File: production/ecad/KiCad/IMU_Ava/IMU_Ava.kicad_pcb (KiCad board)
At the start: 2 copper layers, 8 parts, among them J1 Conn_01x04_Socket, U1 BMI088

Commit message: PCB IMU
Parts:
- moved TP2 10.3 mm to (139.5, 88.5)
- moved C1 9.67 mm to (133.0, 90.0), turned to 180 degrees
- moved R1 9.65 mm to (143.0, 90.0)
- moved C2 9.58 mm to (133.0, 93.5), turned to 180 degrees
- moved R2 9.26 mm to (143.0, 93.5)
- moved J1 8.09 mm to (141.8, 85.0), turned to 180 degrees
- moved TP1 5.69 mm to (136.5, 88.5)
- moved U1 1.04 mm to (138.0, 92.9), turned to 90 degrees
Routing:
- net +3.3V: track 0.00 -> 11.5 mm
- net GND: track 0.00 -> 10.5 mm, vias 0 -> 4
- net /SDA: track 0.00 -> 7.36 mm
- net /SCL: track 0.00 -> 6.72 mm
- net Net-(U1-SDO2): track 0.00 -> 3.63 mm
- net Net-(U1-SDO1): track 0.00 -> 3.21 mm
- added copper zone on F.Cu, net +3.3V
- added copper zone on B.Cu, net GND

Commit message: silkscreen IMU PCB
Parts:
- added G***: LOGO, LOGO, B.Cu at (142.9, 93.4)
- added G***: LOGO, LOGO, B.Cu at (136.9, 89.4)

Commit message: add schematic, pullup resistors
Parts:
- added R3: 10k, Resistor_SMD:R_0805_2012Metric_Pad1.20x1.40mm_HandSolder, B.Cu at (136.0, 88.8)
- added R4: 10k, Resistor_SMD:R_0805_2012Metric_Pad1.20x1.40mm_HandSolder, B.Cu at (140.0, 88.8)
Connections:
- U1 pad 14: +3.3V -> Net-(U1-CSB1)
- U1 pad 7: +3.3V -> Net-(U1-PS)
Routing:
- net Net-(U1-CSB1): track 0.00 -> 5.11 mm, vias 0 -> 1
- net Net-(U1-PS): track 0.00 -> 2.61 mm, vias 0 -> 1
- net +3.3V: track 11.5 -> 9.08 mm, vias 0 -> 2
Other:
- board outline added: 15 x 13.5 mm

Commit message: small fixes IMU board
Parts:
- removed the G*** at (142.9, 93.4)

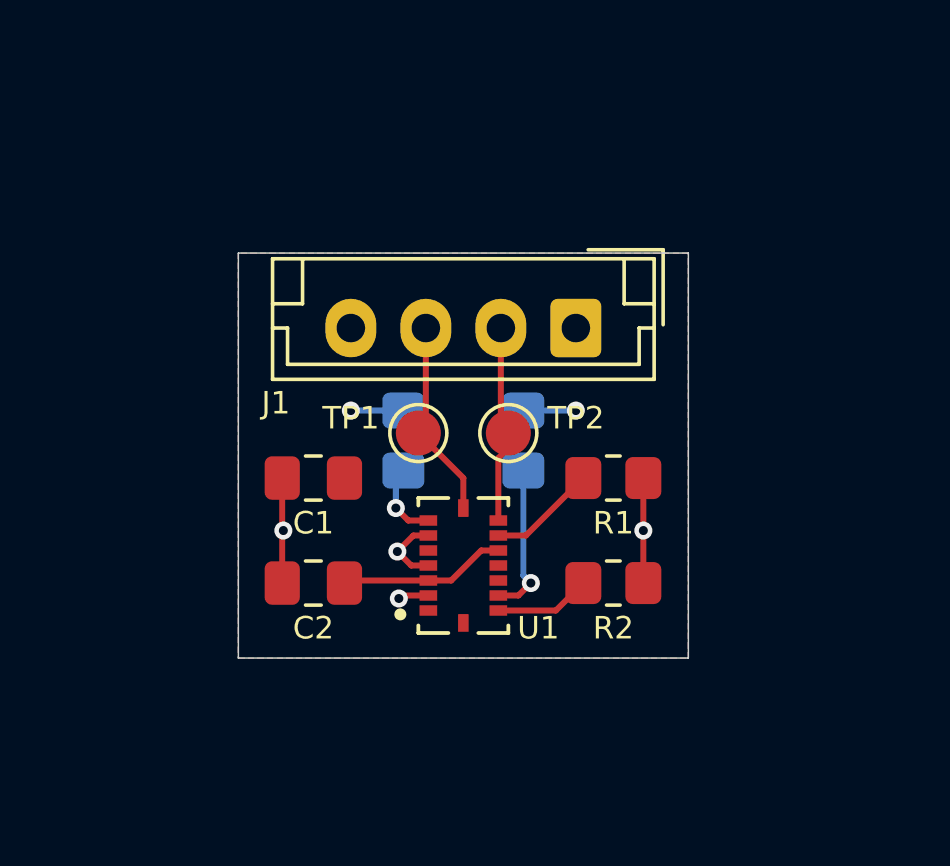
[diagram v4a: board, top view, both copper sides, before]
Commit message: IMU 90 deg conn, fixes
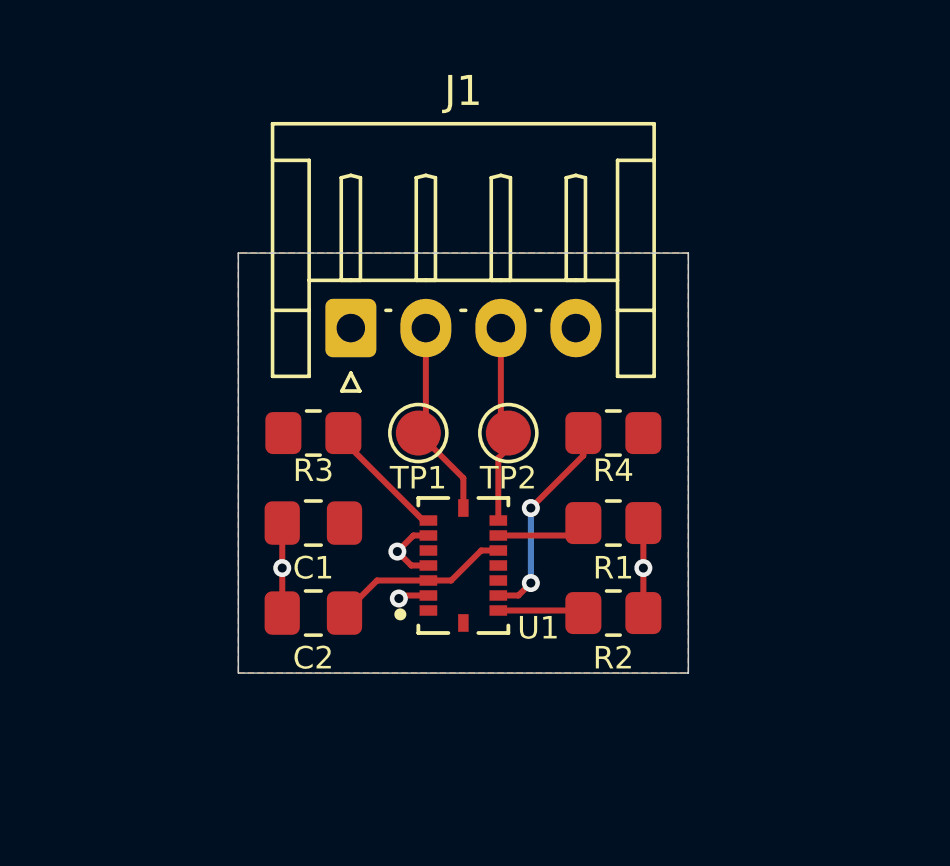
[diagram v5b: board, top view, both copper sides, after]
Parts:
- J1: footprint Connector_JST:JST_EH_B4B-EH-A_1x04_P2.50mm_Vertical -> Connector_JST:JST_EH_S4B-EH_1x04_P2.50mm_Horizontal
- R3, R4: moved to F.Cu
- moved J1 7.50 mm to (134.2, 85.0), turned to 0 degrees
- moved R3 3.01 mm to (133.0, 88.5), turned to 0 degrees
- moved R4 3.01 mm to (143.0, 88.5), turned to 180 degrees
- moved C1 1.50 mm to (133.0, 91.5)
- moved R1 1.50 mm to (143.0, 91.5)
- moved G*** 1.10 mm to (137.0, 90.5)
- moved C2 1.00 mm to (133.0, 94.5)
- moved R2 1.00 mm to (143.0, 94.5)
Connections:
- J1 pad 2: /SDA -> /SCL
- J1 pad 3: /SCL -> /SDA
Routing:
- net +3.3V: track 9.08 -> 5.89 mm, vias 2 -> 0
- net Net-(U1-CSB1): track 5.11 -> 6.98 mm, vias 1 -> 2
- net Net-(U1-PS): track 2.61 -> 3.94 mm, vias 1 -> 0
- net GND: track 10.5 -> 9.51 mm
- net Net-(U1-SDO2): track 3.63 -> 3.01 mm
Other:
- board size 15 x 13.5 mm -> 15 x 14 mm

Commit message: added mounting holes and fixed warnings
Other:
- board size 15 x 14 mm -> 27.1 x 23.9 mm
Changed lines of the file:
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@@
 			(effects
 				(font
-					(size 0.75 0.75)
+					(size 0.8 0.8)
 					(thickness 0.1)
 				)
@@
 			(effects
 				(font
-					(size 0.75 0.75)
+					(size 0.8 0.8)
 					(thickness 0.1)
 				)
@@
 		(tags "connector JST EH horizontal")
 		(property "Reference" "J1"
-			(at 3.75 -7.9 0)
+			(at 3.68 -4.91 0)
 			(layer "F.SilkS")
 			(effects
@@
 		(tags "resistor handsolder")
 		(property "Reference" "R4"
-			(at 0 -1.25 180)
+			(at 0 -1.49 180)
 			(layer "F.SilkS")
 			(effects
 				(font
-					(size 0.75 0.75)
+					(size 0.8 0.8)
 					(thickness 0.1)
 				)
@@
 		(at 138 92.915 90)
 		(property "Reference" "U1"
-			(at -2.085 2.5 180)
+			(at -3.045 0.06 180)
 			(layer "F.SilkS")
 			(effects
 				(font
-					(size 0.75 0.75)
+					(size 0.8 0.8)
 					(thickness 0.1)
 				)
@@
 		(tags "test point SMD pad")
 		(property "Reference" "TP2"
-			(at 0 1.5 0)
+			(at 0 1.59 0)
 			(layer "F.SilkS")
 			(effects
 				(font
-					(size 0.75 0.75)
+					(size 0.8 0.8)
 					(thickness 0.1)
 				)
@@
 		(tags "resistor handsolder")
 		(property "Reference" "R3"
-			(at 0 1.25 180)
+			(at 0.02 1.51 180)
 			(layer "F.SilkS")
 			(effects
 				(font
-					(size 0.75 0.75)
+					(size 0.8 0.8)
 					(thickness 0.1)
 				)
@@
 		(tags "test point SMD pad")
 		(property "Reference" "TP1"
-			(at 0 1.5 0)
+			(at 0 1.64 0)
 			(layer "F.SilkS")
 			(effects
 				(font
-					(size 0.75 0.75)
+					(size 0.8 0.8)
 					(thickness 0.1)
 				)
@@
 			(effects
 				(font
-					(size 0.75 0.75)
+					(size 0.8 0.8)
 					(thickness 0.1)
 				)
@@
 			(effects
 				(font
-					(size 0.75 0.75)
+					(size 0.8 0.8)
 					(thickness 0.1)
 				)
@@
 		)
 	)
+	(gr_circle
+		(center 148.36 97.2)
+		(end 150.23 98.45)
+		(stroke
+			(width 0.05)
+			(type default)
+		)
+		(fill none)
+		(layer "Edge.Cuts")
+	)
 	(gr_rect
-		(start 130.5 82.5)
-		(end 145.5 96.5)
+		(start 124.58 76.65)
+		(end 151.7 100.53)
+		(stroke
+			(width 0.05)
+			(type default)
+		)
+		(fill none)
+		(layer "Edge.Cuts")
+	)
+	(gr_circle
+		(center 148.3 80.07)
+		(end 150.17 81.32)
+		(stroke
+			(width 0.05)
+			(type default)
+		)
+		(fill none)
+		(layer "Edge.Cuts")
+	)
+	(gr_circle
+		(center 128.2 79.96)
+		(end 130.07 81.21)
+		(stroke
+			(width 0.05)
+			(type default)
+		)
+		(fill none)
+		(layer "Edge.Cuts")
+	)
+	(gr_circle
+		(center 128.2 97.2)
+		(end 130.07 98.45)
 		(stroke
 			(width 0.05)
@@
 		(polygon
 			(pts
-				(xy 130.5 82.5) (xy 130.5 96.5) (xy 145.5 96.5) (xy 145.5 82.5)
+				(xy 124.98 76.55) (xy 124.56 100.32) (xy 151.71 100.93) (xy 152.21 77.06)
 			)
 		)
